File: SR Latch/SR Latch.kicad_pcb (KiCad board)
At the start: 2 copper layers, 51 x 38 mm, 17 parts, among them J1 Conn_01x02, Q1 BC547, Q2 BC547, Q3 BC547, Q4 BC547, SW1 RESET, SW2 SET

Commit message: fix(SR Latch): Updated resistor values
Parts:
- R2, R3, R5, R6: value 100K -> 10K
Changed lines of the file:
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@@
         (effects (font (size 1 1) (thickness 0.15)))
     )
-    (fp_text value "100K" (at 0 -3 90) (layer "F.SilkS")
+    (fp_text value "10K" (at 0 -3 90) (layer "F.SilkS")
         (effects (font (size 1 1) (thickness 0.15)))
     )
@@
         (effects (font (size 1 1) (thickness 0.15)))
     )
-    (fp_text value "100K" (at 0 -3) (layer "F.SilkS")
+    (fp_text value "10K" (at 0 -3) (layer "F.SilkS")
         (effects (font (size 1 1) (thickness 0.15)))
     )
@@
     (property "ki_keywords" "R res resistor")
     (attr through_hole)
-    (fp_text reference "R5" (at 0 3) (layer "F.SilkS")
-        (effects (font (size 1 1) (thickness 0.15)))
-    )
-    (fp_text value "100K" (at 0 -3) (layer "F.SilkS")
+    (fp_text reference "R5" (at 0 -3 180) (layer "F.SilkS")
+        (effects (font (size 1 1) (thickness 0.15)))
+    )
+    (fp_text value "10K" (at 0 3 180) (layer "F.SilkS")
         (effects (font (size 1 1) (thickness 0.15)))
     )
@@
         (effects (font (size 1 1) (thickness 0.15)))
     )
-    (fp_text value "100K" (at 0 -3 90) (layer "F.SilkS")
+    (fp_text value "10K" (at 0 -3 90) (layer "F.SilkS")
         (effects (font (size 1 1) (thickness 0.15)))
     )
@@
     (property "ki_keywords" "R res resistor")
     (attr through_hole)
-    (fp_text reference "R4" (at 0 3) (layer "F.SilkS")
-        (effects (font (size 1 1) (thickness 0.15)))
-    )
-    (fp_text value "1K" (at 0 -3) (layer "F.SilkS")
-        (effects (font (size 1 1) (thickness 0.15)))
-    )
+    (fp_text reference "R4" (at 0 -3 180) (layer "F.SilkS")
+        (effects (font (size 1 1) (thickness 0.15)))
+    )
+    (fp_text value "1K" (at 0 3 180) (layer "F.SilkS")
+        (effects (font (size 1 1) (thickness 0.15)))
+    )

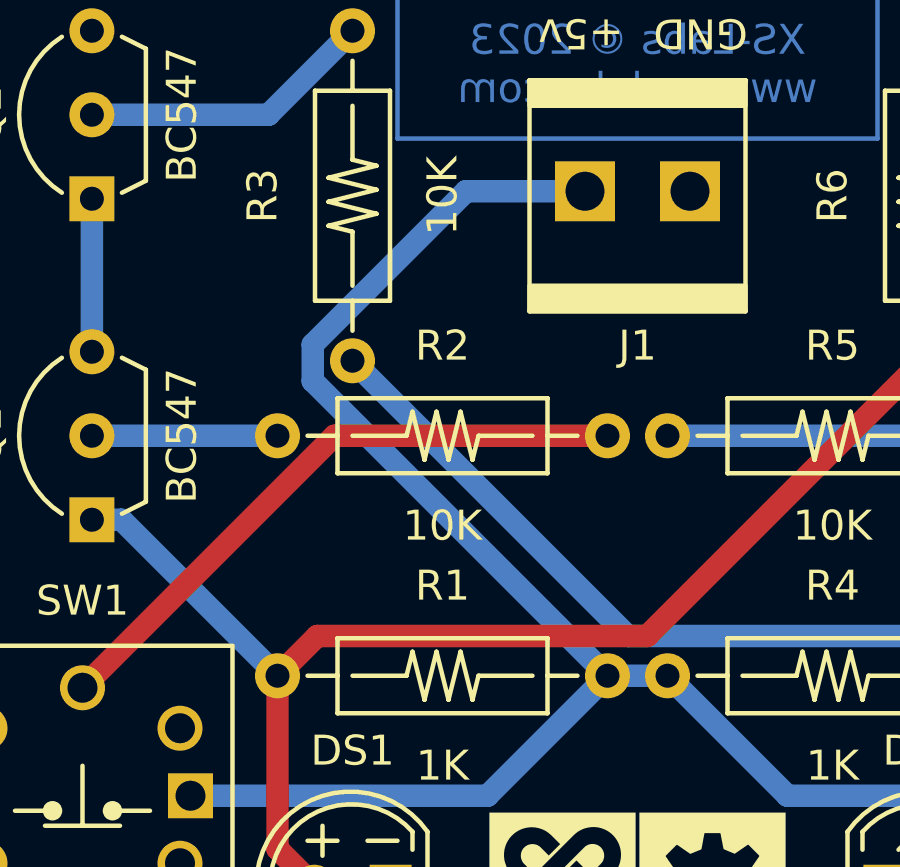
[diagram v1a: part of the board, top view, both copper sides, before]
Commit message: fix: DRC fixes
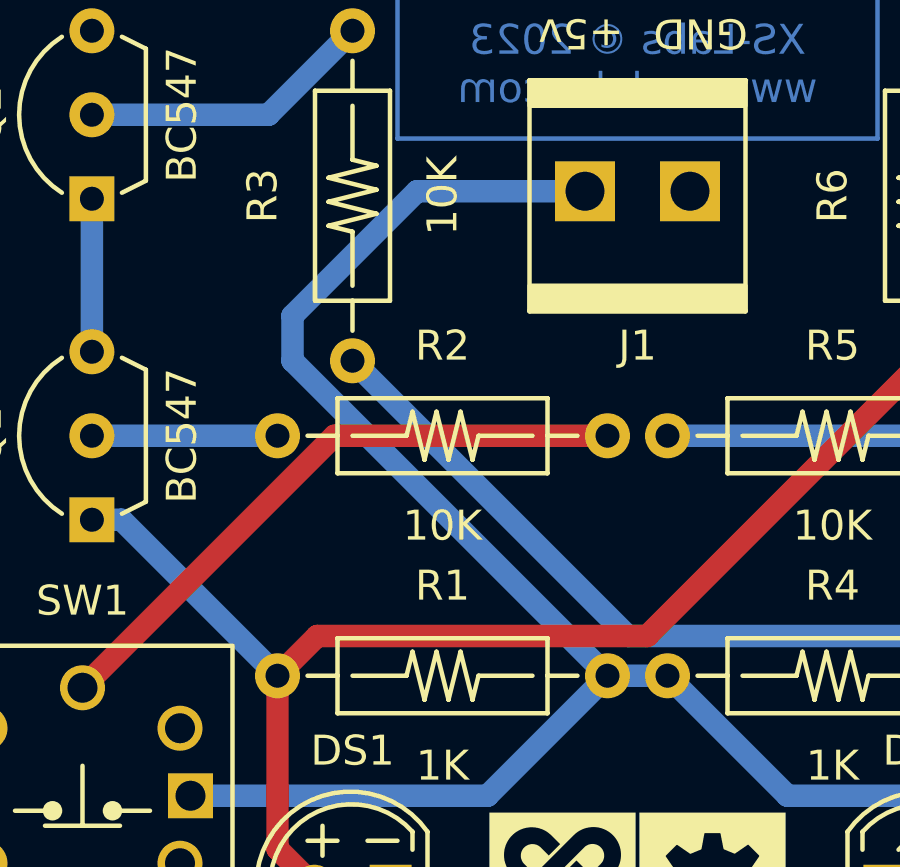
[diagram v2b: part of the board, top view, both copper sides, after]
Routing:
- net VCC: track 67.4 -> 68.9 mm
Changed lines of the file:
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@@
   )
   (segment (start 115.5 57) (end 119.5 61) (width 0.75) (layer "B.Cu") (net 2))
-  (segment (start 112.75 40.85) (end 108.782836 40.85) (width 0.75) (layer "B.Cu") (net 2))
-  (segment (start 108.782836 40.85) (end 103.675 45.957836) (width 0.75) (layer "B.Cu") (net 2))
+  (segment (start 107.15 40.85) (end 103 45) (width 0.75) (layer "B.Cu") (net 2))
   (segment (start 112.175 41.425) (end 112.75 40.85) (width 0.75) (layer "B.Cu") (net 2))
   (segment (start 109.5 61) (end 99.6 61) (width 0.75) (layer "B.Cu") (net 2))
-  (segment (start 103.675 45.957836) (end 103.675 47.175) (width 0.75) (layer "B.Cu") (net 2))
-  (segment (start 103.675 47.175) (end 113.5 57) (width 0.75) (layer "B.Cu") (net 2))
   (segment (start 113.5 57) (end 109.5 61) (width 0.75) (layer "B.Cu") (net 2))
+  (segment (start 112.75 40.85) (end 107.15 40.85) (width 0.75) (layer "B.Cu") (net 2))
+  (segment (start 103 46.5) (end 113.5 57) (width 0.75) (layer "B.Cu") (net 2))
   (segment (start 119.5 61) (end 136.6 61) (width 0.75) (layer "B.Cu") (net 2))
   (segment (start 115.5 57) (end 113.5 57) (width 0.75) (layer "B.Cu") (net 2))
+  (segment (start 103 45) (end 103 46.5) (width 0.75) (layer "B.Cu") (net 2))
   (segment (start 96.313205 49) (end 102.5 49) (width 0.75) (layer "B.Cu") (net 3))
   (segment (start 96.313205 41.1) (end 96.313205 46.2) (width 0.75) (layer "B.Cu") (net 4))

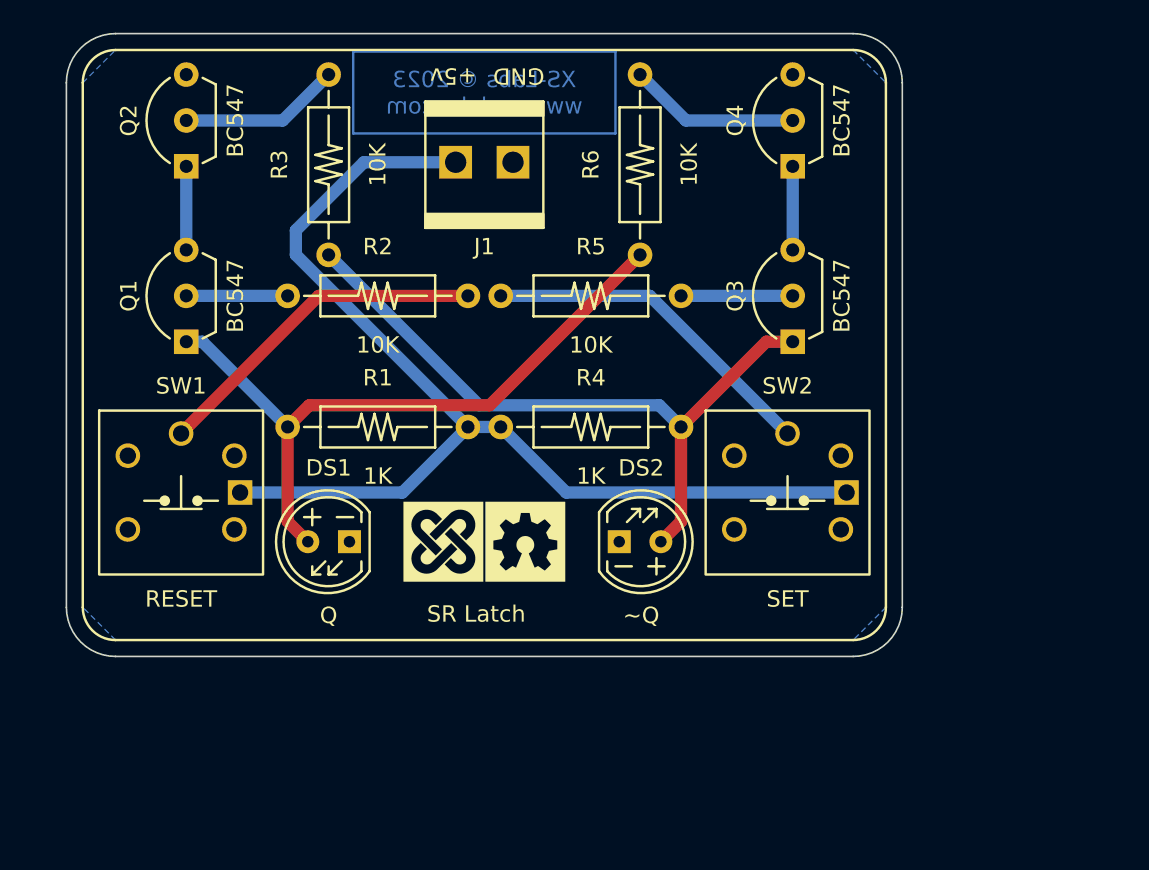
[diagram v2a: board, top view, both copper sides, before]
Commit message: fix: Fixed the SR Latch project (Omron tactile switches)
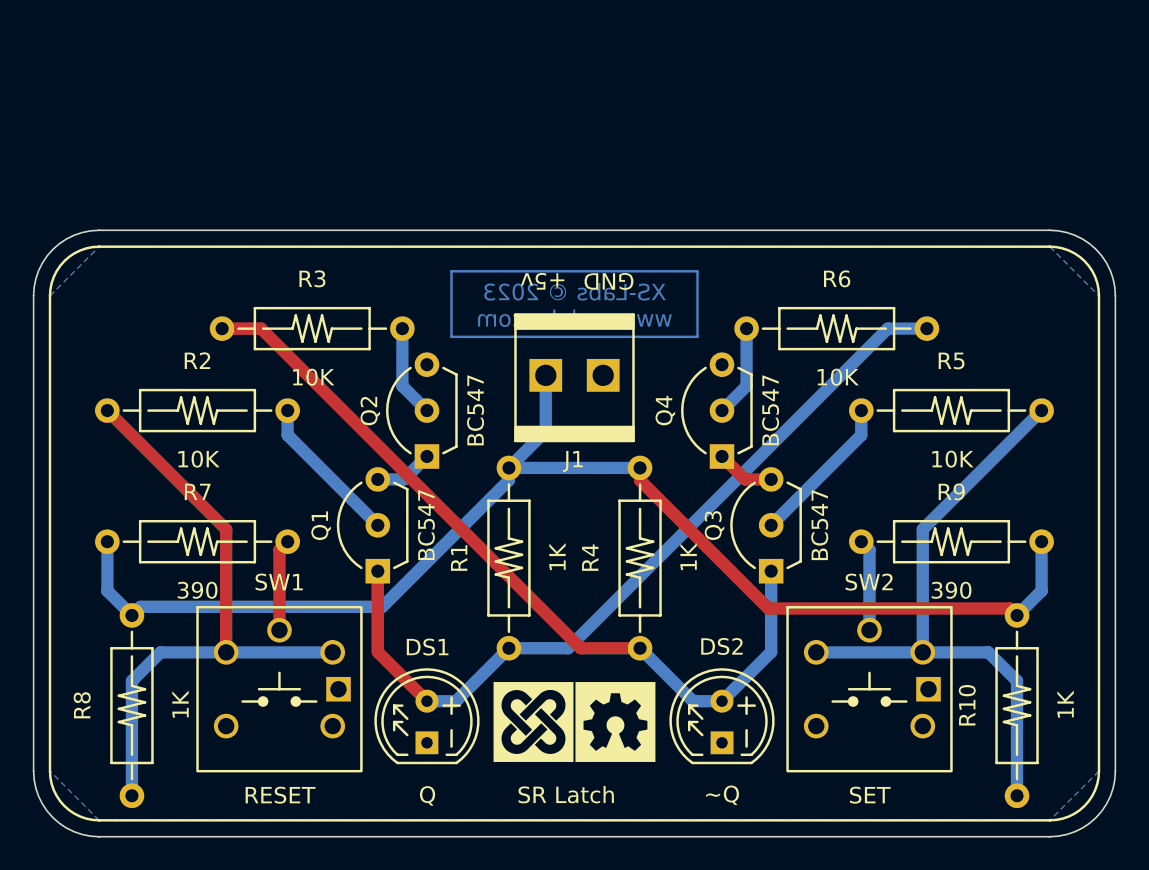
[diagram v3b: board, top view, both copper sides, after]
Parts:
- added R10: 1K, XS:Resistor-Vishay-CCF07, F.Cu at (147.0, 74.0)
- added R7: 390, XS:Resistor-Vishay-CCF07, F.Cu at (97.0, 64.0)
- added R8: 1K, XS:Resistor-Vishay-CCF07, F.Cu at (93.0, 74.0)
- added R9: 390, XS:Resistor-Vishay-CCF07, F.Cu at (143.0, 64.0)
- SW1, SW2: footprint XS:Tactile-Omrom-B3W-900X-X1X -> XS:Tactile-Omron-B3W-900X-X1X
- moved R5 23.1 mm to (143.0, 56.0), turned to 180 degrees
- moved Q2 23.0 mm to (111.0, 56.0)
- moved Q1 18.2 mm to (108.0, 63.0)
- moved Q4 18.2 mm to (129.0, 56.0)
- moved R6 15.6 mm to (136.0, 51.0), turned to 0 degrees
- moved J1 14.1 mm to (120.0, 54.0)
- moved Q3 14.1 mm to (132.0, 63.0)
- moved SW1 13.4 mm to (102.0, 73.0)
- moved R2 13.0 mm to (97.0, 56.0), turned to 0 degrees
- moved SW2 13.0 mm to (138.0, 73.0)
- moved DS1 12.5 mm to (111.0, 75.0), turned to 90 degrees
- moved G*** 12.3 mm to (117.5, 75.0)
- moved G*** 12.3 mm to (122.5, 75.0)
- moved DS2 12.1 mm to (129.0, 75.0), turned to 90 degrees
- moved R1 11.3 mm to (116.0, 65.0), turned to -90 degrees
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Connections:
- net Net-(DS1-A) renamed Q
- net Net-(DS2-A) renamed ~Q
- R2 pad 1: Net-(SW1-B) -> A
- R5 pad 1: Net-(SW2-B) -> B
- SW1 pad 1: VCC -> GND
- SW1 pad 2: Net-(SW1-B) -> GND
- SW2 pad 1: VCC -> GND
- SW2 pad 2: Net-(SW2-B) -> GND
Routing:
- net B: track 0.00 -> 37.7 mm
- net A: track 0.00 -> 37.7 mm
- net Net-(SW2-B): track 21.0 -> 0.00 mm
- net Net-(SW1-B): track 21.0 -> 0.00 mm
- net VCC: track 68.9 -> 79.2 mm
- net Q: track 41.7 -> 49.1 mm
- net ~Q: track 42.3 -> 49.1 mm
- net Net-(SW2-A): track 0.00 -> 5.61 mm
- net Net-(SW1-A): track 0.00 -> 5.61 mm
- net Net-(Q4-B): track 10.5 -> 5.62 mm
- net Net-(Q2-B): track 9.85 -> 5.62 mm
- net Net-(Q1-B): track 6.19 -> 9.28 mm
- net Net-(Q3-B): track 6.81 -> 9.28 mm
- net Net-(Q3-E): track 5.10 -> 3.58 mm
- net Net-(Q1-E): track 5.10 -> 3.58 mm
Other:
- board size 51 x 38 mm -> 66 x 37 mm

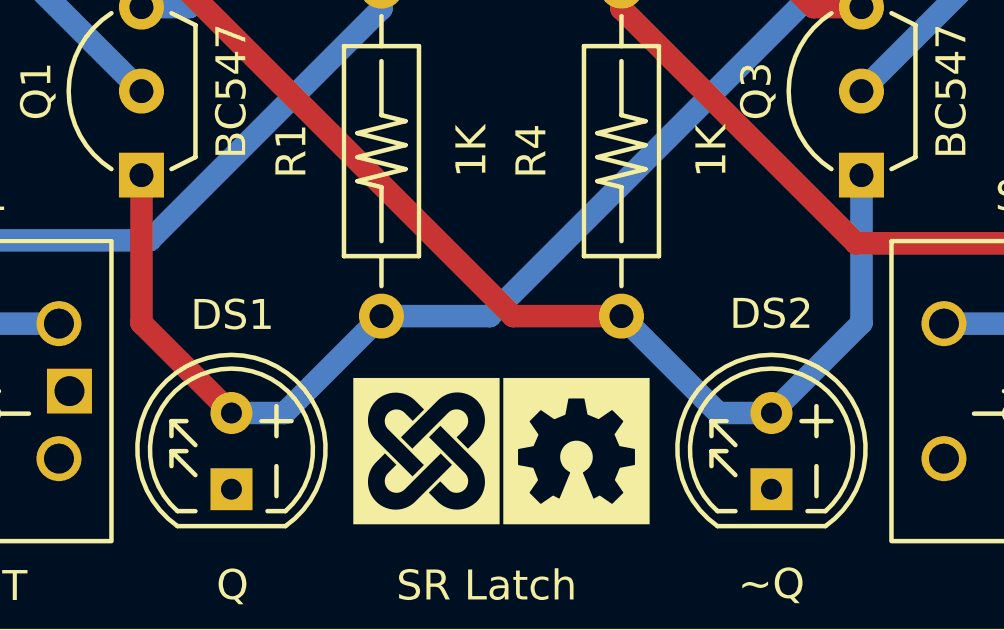
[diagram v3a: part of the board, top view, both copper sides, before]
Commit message: chore: Using D for LEDs instead of DS
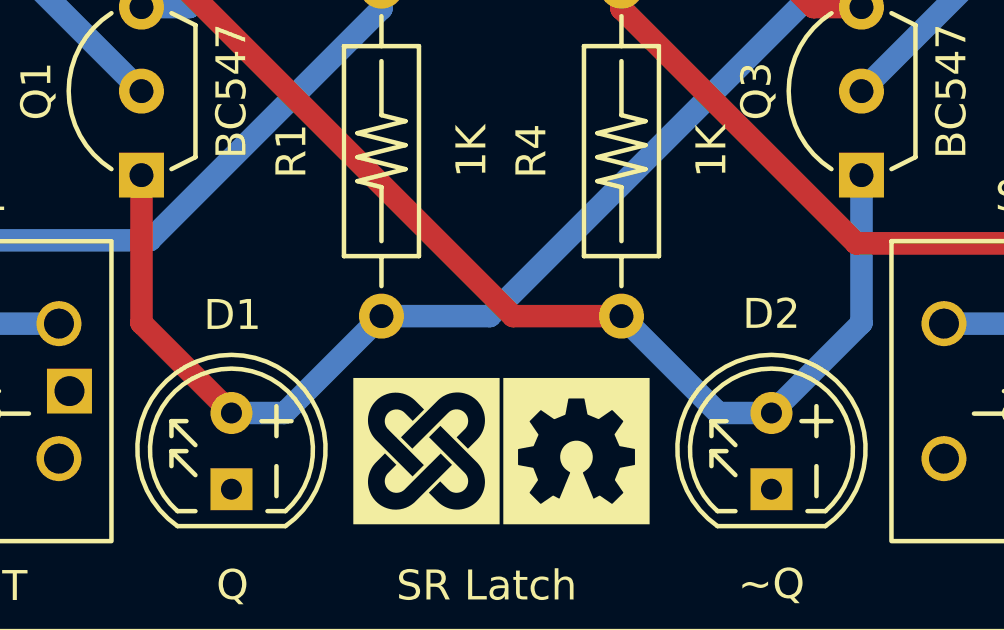
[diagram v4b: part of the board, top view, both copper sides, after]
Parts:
- renumbered DS1 to D1, DS2 to D2
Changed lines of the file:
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@@
     (property "ki_keywords" "LED diode")
     (attr through_hole)
-    (fp_text reference "DS1" (at 4.53453 0.03453 180) (layer "F.SilkS")
+    (fp_text reference "D1" (at 4.53453 0.03453 180) (layer "F.SilkS")
         (effects (font (size 1 1) (thickness 0.15)))
     )
@@
     (property "ki_keywords" "LED diode")
     (attr through_hole)
-    (fp_text reference "DS2" (at 4.570664 -0.001604 180) (layer "F.SilkS")
-        (effects (font (size 1 1) (thickness 0.15)))
-    )
+    (fp_text reference "D2" (at 4.570664 -0.001604 180) (layer "F.SilkS")
+        (effects (font (size 1 1) (thickness 0.15)))
+    )

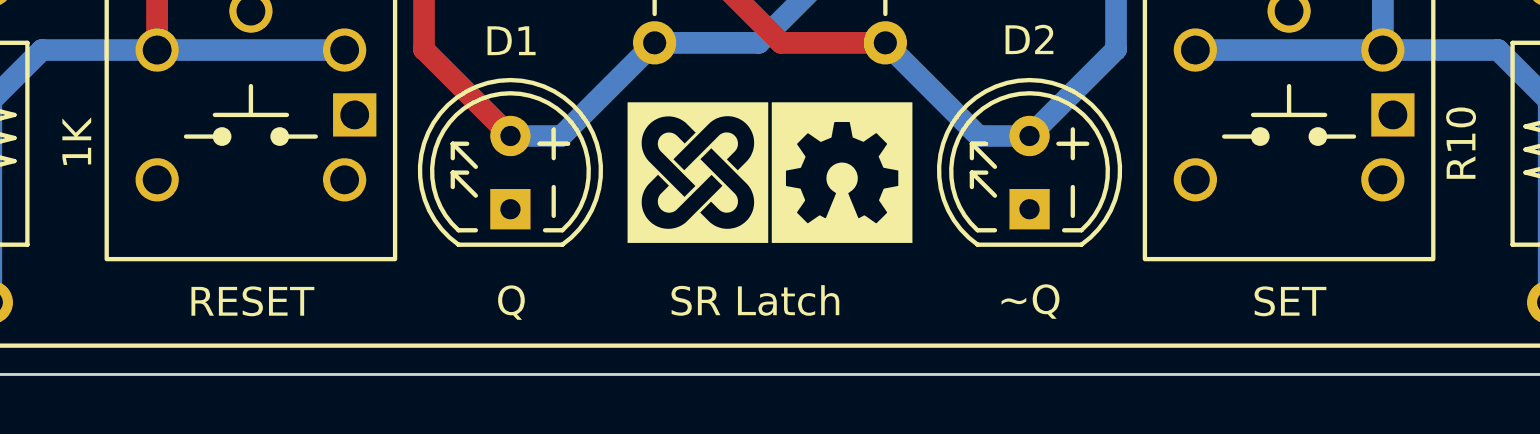
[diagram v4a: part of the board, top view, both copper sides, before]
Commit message: fix: SR Latch - Fixed the SET/RESET labels
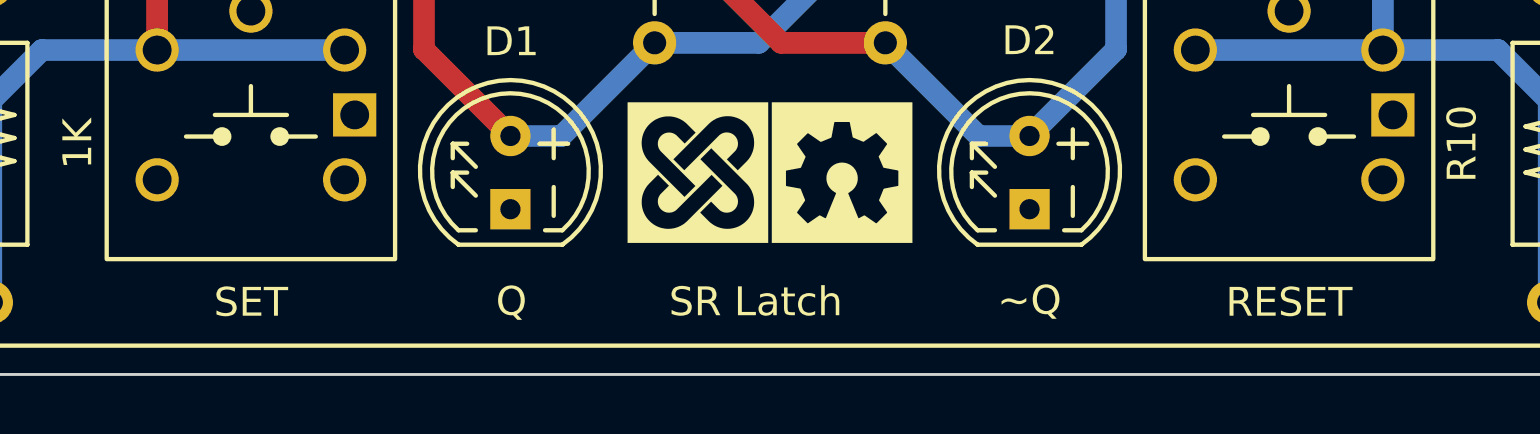
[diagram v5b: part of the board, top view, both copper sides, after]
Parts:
- SW1: value RESET -> SET
- SW2: value SET -> RESET
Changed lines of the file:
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@@
         (effects (font (size 1 1) (thickness 0.15)))
     )
-    (fp_text value "RESET" (at 0 6.5 180) (layer "F.SilkS")
+    (fp_text value "SET" (at 0 6.5 180) (layer "F.SilkS")
         (effects (font (size 1 1) (thickness 0.15)))
     )
@@
         (effects (font (size 1 1) (thickness 0.15)))
     )
-    (fp_text value "SET" (at 0 6.5 180) (layer "F.SilkS")
+    (fp_text value "RESET" (at 0 6.5 180) (layer "F.SilkS")
         (effects (font (size 1 1) (thickness 0.15)))
     )
